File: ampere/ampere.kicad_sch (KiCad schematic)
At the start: 24 parts, among them J1 USB_C_Receptacle, J5 2x12 IDC, U2 STM32G474RETx, Y1 25 MHZ, Y2 32.768 KHZ

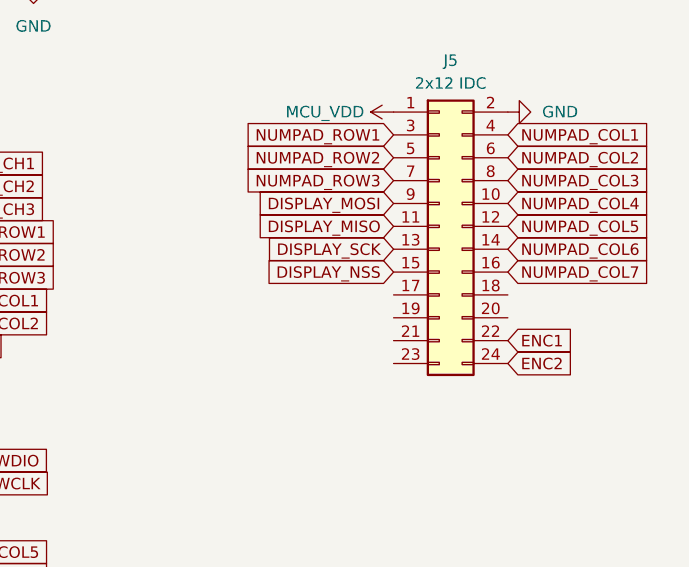
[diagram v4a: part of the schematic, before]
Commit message: add keypad matrix traces, pour out prelim PPHV copper
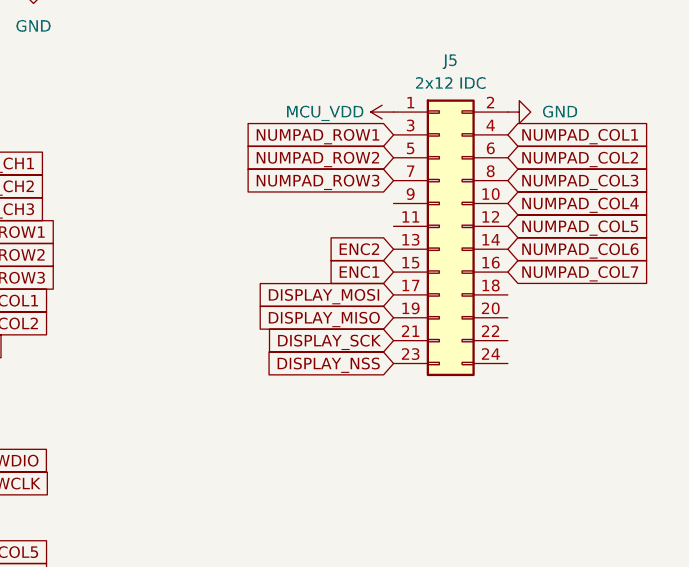
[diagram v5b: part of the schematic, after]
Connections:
- net DISPLAY_MISO: now also J5.19 (Pin_19); no longer J5.11 (Pin_11)
- net DISPLAY_MOSI: now also J5.17 (Pin_17); no longer J5.9 (Pin_9)
- net DISPLAY_NSS: now also J5.23 (Pin_23); no longer J5.15 (Pin_15)
- net DISPLAY_SCK: now also J5.21 (Pin_21); no longer J5.13 (Pin_13)
- net ENC1: now also J5.15 (Pin_15); no longer J5.22 (Pin_22)
- net ENC2: now also J5.13 (Pin_13); no longer J5.24 (Pin_24)

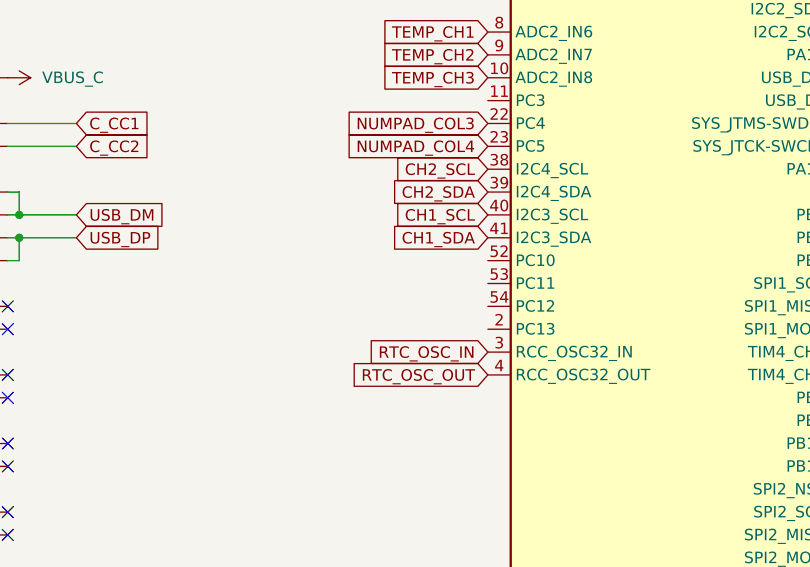
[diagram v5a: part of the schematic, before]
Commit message: finalize display interconnect corridor
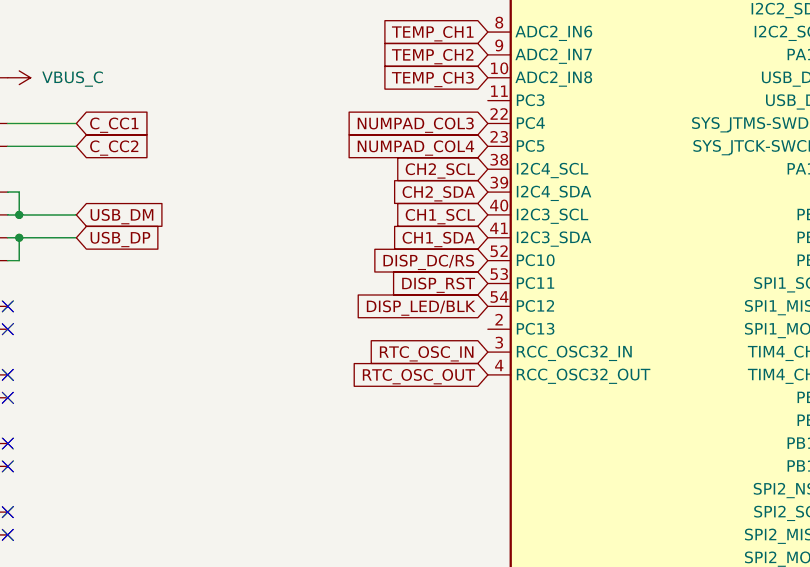
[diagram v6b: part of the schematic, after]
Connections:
- net DISP_DC/RS: now reaches U2.52 (PC10)
- net DISP_RST: now reaches U2.53 (PC11)
- net DISP_LED/BLK: now reaches U2.54 (PC12)
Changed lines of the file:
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@@
+		)
+	)
+	(global_label "DISP_LED/BLK"
+		(shape input)
+		(at 129.54 121.92 180)
+		(fields_autoplaced yes)
+		(effects
+			(font
+				(size 1.27 1.27)
+			)
+			(justify right)
+		)
+		(property "Intersheetrefs" "${INTERSHEET_REFS}"
+			(at 124.0753 121.92 0)
+			(hide yes)
+			(show_name no)
+			(do_not_autoplace no)
+			(effects
+				(font
+					(size 1.27 1.27)
+				)
+				(justify right)
+			)
 		)
 	)
@@
 		)
 	)
+	(global_label "DISP_DC/RS"
+		(shape input)
+		(at 129.54 116.84 180)
+		(fields_autoplaced yes)
+		(effects
+			(font
+				(size 1.27 1.27)
+			)
+			(justify right)
+		)
+		(property "Intersheetrefs" "${INTERSHEET_REFS}"
+			(at 124.0753 116.84 0)
+			(hide yes)
+			(show_name no)
+			(do_not_autoplace no)
+			(effects
+				(font
+					(size 1.27 1.27)
+				)
+				(justify right)
+			)
+		)
+	)
 	(global_label "RTC_OSC_IN"
 		(shape input)
@@
 			)
 		)
+	)
+	(global_label "DISP_RST"
+		(shape input)
+		(at 129.54 119.38 180)
+		(fields_autoplaced yes)
+		(effects
+			(font
+				(size 1.27 1.27)
+			)
+			(justify right)
+		)
+		(property "Intersheetrefs" "${INTERSHEET_REFS}"
+			(at 124.0753 119.38 0)
+			(hide yes)
+			(show_name no)
+			(do_not_autoplace no)
+			(effects
+				(font
+					(size 1.27 1.27)
+				)
+				(justify right)
+			)
+		)

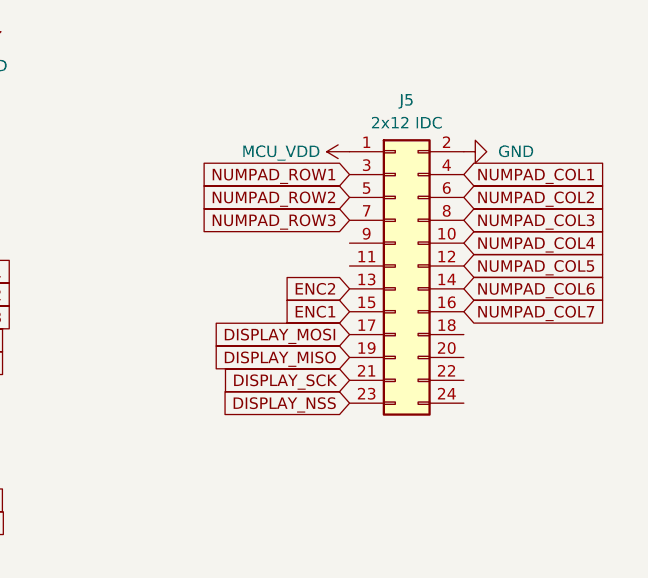
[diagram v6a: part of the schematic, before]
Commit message: begin implementing AGND retrofit
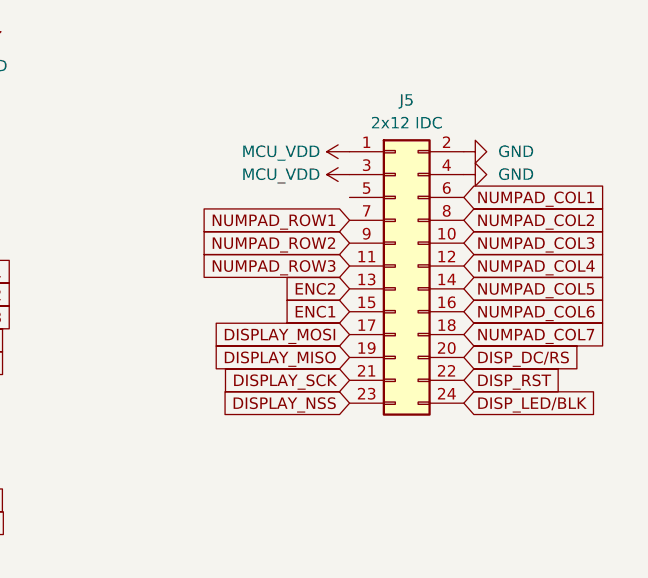
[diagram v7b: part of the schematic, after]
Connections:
- net DISP_DC/RS: now also J5.20 (Pin_20)
- net DISP_LED/BLK: now also J5.24 (Pin_24)
- net DISP_RST: now also J5.22 (Pin_22)
- net GND: now also J5.4 (Pin_4)
- net MCU_VDD: now also J5.3 (Pin_3)
- net NUMPAD_COL1: now also J5.6 (Pin_6); no longer J5.4 (Pin_4)
- net NUMPAD_COL2: now also J5.8 (Pin_8); no longer J5.6 (Pin_6)
- net NUMPAD_COL3: now also J5.10 (Pin_10); no longer J5.8 (Pin_8)
- net NUMPAD_COL4: now also J5.12 (Pin_12); no longer J5.10 (Pin_10)
- net NUMPAD_COL5: now also J5.14 (Pin_14); no longer J5.12 (Pin_12)
- net NUMPAD_COL6: now also J5.16 (Pin_16); no longer J5.14 (Pin_14)
- net NUMPAD_COL7: now also J5.18 (Pin_18); no longer J5.16 (Pin_16)
- net NUMPAD_ROW1: now also J5.7 (Pin_7); no longer J5.3 (Pin_3)
- net NUMPAD_ROW2: now also J5.9 (Pin_9); no longer J5.5 (Pin_5)
- net NUMPAD_ROW3: now also J5.11 (Pin_11); no longer J5.7 (Pin_7)
